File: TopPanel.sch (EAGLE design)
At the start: 19 parts

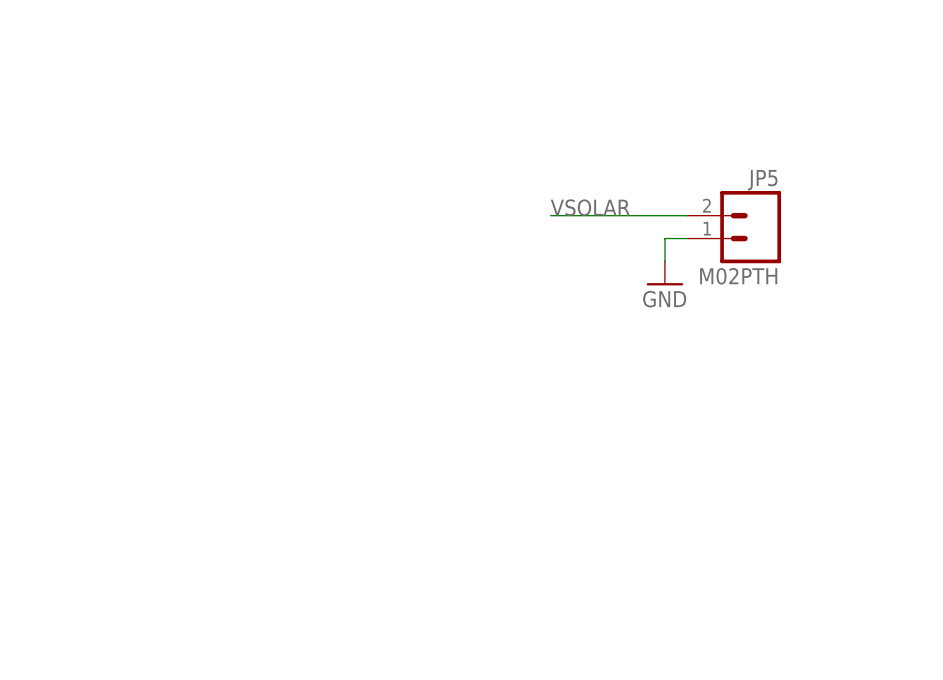
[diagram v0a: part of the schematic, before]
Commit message: Connector swap
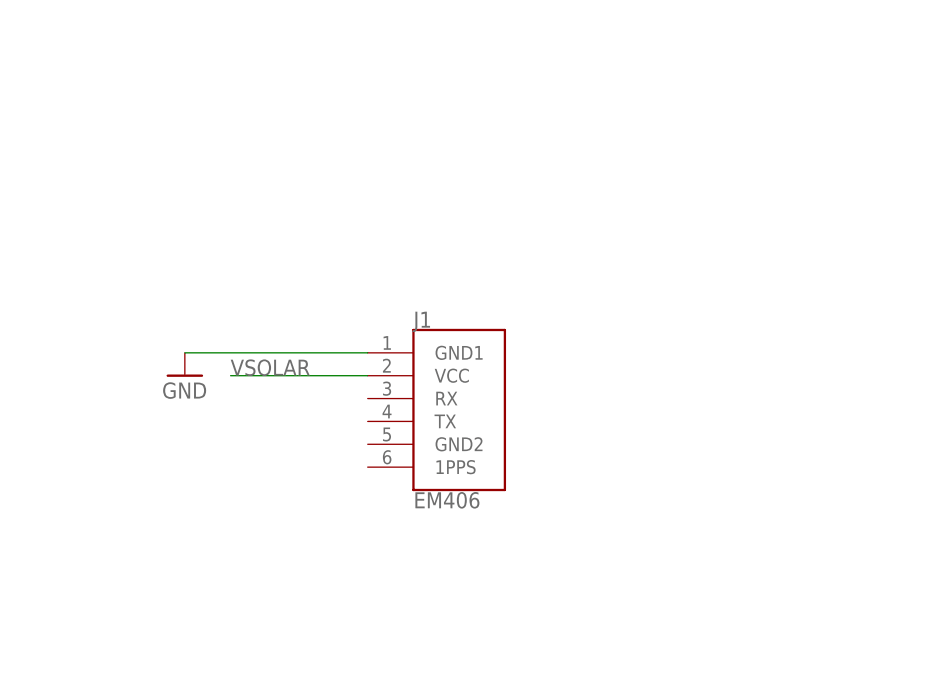
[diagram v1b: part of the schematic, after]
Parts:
- removed JP5: M02PTH, SparkFun-Connectors:M02PTH
- added J1: EM406, SparkFun-Connectors:EM406
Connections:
- net GND: now also J1.GND1; no longer JP5.1
- net VSOLAR: now also J1.VCC; no longer JP5.2
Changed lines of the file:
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@@
 <?xml version="1.0" encoding="utf-8"?>
 <!DOCTYPE eagle SYSTEM "eagle.dtd">
-<eagle version="8.6.1">
+<eagle version="9.1.3">
 <drawing>
 <settings>
@@
 <layers>
 <layer number="1" name="Top" color="4" fill="1" visible="no" active="no"/>
+<layer number="2" name="Route2" color="1" fill="3" visible="no" active="no"/>
+<layer number="3" name="Route3" color="4" fill="3" visible="no" active="no"/>
+<layer number="4" name="Route4" color="1" fill="4" visible="no" active="no"/>
+<layer number="5" name="Route5" color="4" fill="4" visible="no" active="no"/>
+<layer number="6" name="Route6" color="1" fill="8" visible="no" active="no"/>
+<layer number="7" name="Route7" color="4" fill="8" visible="no" active="no"/>
+<layer number="8" name="Route8" color="1" fill="2" visible="no" active="no"/>
+<layer number="9" name="Route9" color="4" fill="2" visible="no" active="no"/>
+<layer number="10" name="Route10" color="1" fill="7" visible="no" active="no"/>
+<layer number="11" name="Route11" color="4" fill="7" visible="no" active="no"/>
+<layer number="12" name="Route12" color="1" fill="5" visible="no" active="no"/>
+<layer number="13" name="Route13" color="4" fill="5" visible="no" active="no"/>
+<layer number="14" name="Route14" color="1" fill="6" visible="no" active="no"/>
+<layer number="15" name="Route15" color="4" fill="6" visible="no" active="no"/>
 <layer number="16" name="Bottom" color="1" fill="1" visible="no" active="no"/>
 <layer number="17" name="Pads" color="2" fill="1" visible="no" active="no"/>
@@
 <layer number="54" name="bGND_GNDA" color="1" fill="9" visible="no" active="no"/>
 <layer number="56" name="wert" color="7" fill="1" visible="no" active="no"/>
+<layer number="57" name="tCAD" color="7" fill="1" visible="no" active="no"/>
+<layer number="59" name="tCarbon" color="7" fill="1" visible="no" active="no"/>
+<layer number="60" name="bCarbon" color="7" fill="1" visible="no" active="no"/>
 <layer number="88" name="SimResults" color="9" fill="1" visible="yes" active="yes"/>
 <layer number="89" name="SimProbes" color="9" fill="1" visible="yes" active="yes"/>
@@
 <layer number="97" name="Info" color="7" fill="1" visible="yes" active="yes"/>
 <layer number="98" name="Guide" color="6" fill="1" visible="yes" active="yes"/>
+<layer number="99" name="SpiceOrder" color="7" fill="1" visible="yes" active="yes"/>
 <layer number="100" name="Muster" color="7" fill="1" visible="no" active="no"/>
 <layer number="101" name="Patch_Top" color="12" fill="4" visible="yes" active="yes"/>
@@
 <layer number="112" name="tSilk" color="7" fill="1" visible="yes" active="yes"/>
 <layer number="113" name="IDFDebug" color="4" fill="1" visible="yes" active="yes"/>
+<layer number="114" name="Badge_Outline" color="7" fill="1" visible="yes" active="yes"/>
+<layer number="115" name="ReferenceISLANDS" color="7" fill="1" visible="yes" active="yes"/>
 <layer number="116" name="Patch_BOT" color="9" fill="4" visible="yes" active="yes"/>
+<layer number="118" name="Rect_Pads" color="7" fill="1" visible="yes" active="yes"/>
 <layer number="121" name="_tsilk" color="7" fill="1" visible="yes" active="yes"/>
 <layer number="122" name="_bsilk" color="7" fill="1" visible="yes" active="yes"/>
@@
 <layer number="127" name="_tValues" color="7" fill="1" visible="yes" active="yes"/>
 <layer number="128" name="_bValues" color="7" fill="1" visible="yes" active="yes"/>
+<layer number="129" name="Mask" color="7" fill="1" visible="yes" active="yes"/>
 <layer number="131" name="tAdjust" color="7" fill="1" visible="yes" active="yes"/>
 <layer number="132" name="bAdjust" color="7" fill="1" visible="yes" active="yes"/>
 <layer number="144" name="Drill_legend" color="7" fill="1" visible="yes" active="yes"/>
+<layer number="150" name="Notes" color="7" fill="1" visible="yes" active="yes"/>
 <layer number="151" name="HeatSink" color="7" fill="1" visible="yes" active="yes"/>
 <layer number="152" name="_bDocu" color="7" fill="1" visible="yes" active="yes"/>
+<layer number="153" name="FabDoc1" color="7" fill="1" visible="yes" active="yes"/>
+<layer number="154" name="FabDoc2" color="7" fill="1" visible="yes" active="yes"/>
+<layer number="155" name="FabDoc3" color="7" fill="1" visible="yes" active="yes"/>
 <layer number="199" name="Contour" color="7" fill="1" visible="yes" active="yes"/>
 <layer number="200" name="200bmp" color="1" fill="10" visible="yes" active="yes"/>
@@
 <layer number="223" name="223bmp" color="24" fill="1" visible="no" active="no"/>
 <layer number="224" name="224bmp" color="25" fill="1" visible="no" active="no"/>
+<layer number="225" name="225bmp" color="7" fill="1" visible="yes" active="yes"/>
+<layer number="226" name="226bmp" color="7" fill="1" visible="yes" active="yes"/>
+<layer number="227" name="227bmp" color="7" fill="1" visible="yes" active="yes"/>
+<layer number="228" name="228bmp" color="7" fill="1" visible="yes" active="yes"/>
+<layer number="229" name="229bmp" color="7" fill="1" visible="yes" active="yes"/>
+<layer number="230" name="230bmp" color="7" fill="1" visible="yes" active="yes"/>
+<layer number="231" name="231bmp" color="7" fill="1" visible="yes" active="yes"/>
+<layer number="232" name="Eagle3D_PG2" color="7" fill="1" visible="yes" active="yes"/>
+<layer number="233" name="Eagle3D_PG3" color="7" fill="1" visible="yes" active="yes"/>
 <layer number="248" name="Housing" color="7" fill="1" visible="yes" active="yes"/>
 <layer number="249" name="Edge" color="7" fill="1" visible="yes" active="yes"/>
@@
 <layer number="251" name="SMDround" color="12" fill="11" visible="no" active="no"/>
 <layer number="254" name="cooling" color="7" fill="1" visible="yes" active="yes"/>
+<layer number="255" name="routoute" color="7" fill="1" visible="yes" active="yes"/>
 </layers>
 <schematic xreflabel="%F%N/%S.%C%R" xrefpart="/%S.%C%R">
@@
 <part name="GND1" library="SparkFun" deviceset="GND" device=""/>
 <part name="FRAME1" library="SparkFun-Aesthetics" deviceset="FRAME-LETTER" device=""/>
-<part name="JP5" library="SparkFun-Connectors" deviceset="M02" device="PTH"/>
-<part name="GND2" library="SparkFun" deviceset="GND" device=""/>
 <part name="U$1" library="KickSat-Logo" deviceset="KICKSAT_LOGO" device=""/>
+<part name="J1" library="SparkFun-Connectors" library_urn="urn:adsk.eagle:library:513" deviceset="EM406" device="" package3d_urn="urn:adsk.eagle:package:38023/1"/>
+<part name="GND3" library="SparkFun" deviceset="GND" device=""/>
 </parts>
 <sheets>
@@
 <instance part="FRAME1" gate="G$1" x="0" y="0"/>
 <instance part="FRAME1" gate="G$2" x="147.32" y="0"/>
-<instance part="JP5" gate="G$1" x="208.28" y="111.76" rot="MR0"/>
-<instance part="GND2" gate="1" x="198.12" y="106.68"/>
 <instance part="U$1" gate="G$1" x="218.44" y="25.4"/>
+<instance part="J1" gate="G$1" x="175.26" y="91.44"/>
+<instance part="GND3" gate="1" x="144.78" y="96.52"/>
 </instances>
 <busses>
@@
 </segment>
 <segment>
-<pinref part="JP5" gate="G$1" pin="2"/>
-<wire x1="200.66" y1="114.3" x2="185.42" y2="114.3" width="0.1524" layer="91"/>
-<label x="185.42" y="114.3" size="1.778" layer="95"/>
+<wire x1="165.1" y1="96.52" x2="149.86" y2="96.52" width="0.1524" layer="91"/>
+<pinref part="J1" gate="G$1" pin="VCC"/>
+<label x="149.86" y="96.52" size="1.778" layer="95"/>
 </segment>
 </net>
@@
 </segment>
 <segment>
-<pinref part="JP5" gate="G$1" pin="1"/>
-<pinref part="GND2" gate="1" pin="GND"/>
-<wire x1="200.66" y1="111.76" x2="198.12" y2="111.76" width="0.1524" layer="91"/>
-<wire x1="198.12" y1="111.76" x2="198.12" y2="109.22" width="0.1524" layer="91"/>
+<pinref part="J1" gate="G$1" pin="GND1"/>
+<pinref part="GND3" gate="1" pin="GND"/>
+<wire x1="165.1" y1="99.06" x2="144.78" y2="99.06" width="0.1524" layer="91"/>
 </segment>
 </net>
@@
 </schematic>
 </drawing>
+<compatibility>
+<note version="8.2" severity="warning">
+Since Version 8.2, EAGLE supports online libraries. The ids
+of those online libraries will not be understood (or retained)
+with this version.
+</note>
+<note version="8.3" severity="warning">
+Since Version 8.3, EAGLE supports URNs for individual library
+assets (packages, symbols, and devices). The URNs of those assets
+will not be understood (or retained) with this version.
+</note>
+<note version="8.3" severity="warning">
+Since Version 8.3, EAGLE supports the association of 3D packages
+with devices in libraries, schematics, and board files. Those 3D
+packages will not be understood (or retained) with this version.
+</note>
+</compatibility>
 </eagle>

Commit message: Started routing
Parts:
- added U$2, U$3, U$4: BURNWIRE, BurnWire:BURNWIRE
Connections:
- new net VBURN1: J1.VCC, U$2.V+
- new net VBURN2: J1.RX, U$3.V+
- new net VBURN3: J1.TX, U$4.V+
- net GND: now also J1.GND2, U$2.V-, U$3.V-, U$4.V-
- net VSOLAR: now also J1.1PPS; no longer J1.VCC
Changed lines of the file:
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@@
 <part name="J1" library="SparkFun-Connectors" library_urn="urn:adsk.eagle:library:513" deviceset="EM406" device="" package3d_urn="urn:adsk.eagle:package:38023/1"/>
 <part name="GND3" library="SparkFun" deviceset="GND" device=""/>
+<part name="GND2" library="SparkFun" deviceset="GND" device=""/>
+<part name="GND4" library="SparkFun" deviceset="GND" device=""/>
+<part name="GND5" library="SparkFun" deviceset="GND" device=""/>
+<part name="GND6" library="SparkFun" deviceset="GND" device=""/>
+<part name="U$2" library="BurnWire" deviceset="BURNWIRE" device=""/>
+<part name="U$3" library="BurnWire" deviceset="BURNWIRE" device=""/>
+<part name="U$4" library="BurnWire" deviceset="BURNWIRE" device=""/>
 </parts>
 <sheets>
@@
 <instance part="J1" gate="G$1" x="175.26" y="91.44"/>
 <instance part="GND3" gate="1" x="144.78" y="96.52"/>
+<instance part="GND2" gate="1" x="144.78" y="86.36"/>
+<instance part="GND4" gate="1" x="111.76" y="58.42"/>
+<instance part="GND5" gate="1" x="111.76" y="48.26"/>
+<instance part="GND6" gate="1" x="111.76" y="38.1"/>
+<instance part="U$2" gate="G$1" x="127" y="60.96"/>
+<instance part="U$3" gate="G$1" x="127" y="50.8"/>
+<instance part="U$4" gate="G$1" x="127" y="40.64"/>
 </instances>
 <busses>
@@
 </segment>
 <segment>
-<wire x1="165.1" y1="96.52" x2="149.86" y2="96.52" width="0.1524" layer="91"/>
-<pinref part="J1" gate="G$1" pin="VCC"/>
-<label x="149.86" y="96.52" size="1.778" layer="95"/>
+<pinref part="J1" gate="G$1" pin="1PPS"/>
+<wire x1="165.1" y1="86.36" x2="149.86" y2="86.36" width="0.1524" layer="91"/>
+<label x="149.86" y="86.36" size="1.778" layer="95"/>
 </segment>
 </net>
@@
 <wire x1="165.1" y1="99.06" x2="144.78" y2="99.06" width="0.1524" layer="91"/>
 </segment>
-</net>
+<segment>
+<pinref part="J1" gate="G$1" pin="GND2"/>
+<wire x1="165.1" y1="88.9" x2="147.32" y2="88.9" width="0.1524" layer="91"/>
+<pinref part="GND2" gate="1" pin="GND"/>
+<wire x1="147.32" y1="88.9" x2="144.78" y2="88.9" width="0.1524" layer="91"/>
+</segment>
+<segment>
+<pinref part="GND4" gate="1" pin="GND"/>
+<wire x1="114.3" y1="60.96" x2="111.76" y2="60.96" width="0.1524" layer="91"/>
+<pinref part="U$2" gate="G$1" pin="V-"/>
+</segment>
+<segment>
+<pinref part="GND5" gate="1" pin="GND"/>
+<wire x1="114.3" y1="50.8" x2="111.76" y2="50.8" width="0.1524" layer="91"/>
+<pinref part="U$3" gate="G$1" pin="V-"/>
+</segment>
+<segment>
+<pinref part="GND6" gate="1" pin="GND"/>
+<wire x1="114.3" y1="40.64" x2="111.76" y2="40.64" width="0.1524" layer="91"/>
+<pinref part="U$4" gate="G$1" pin="V-"/>
+</segment>
+</net>
+<net name="VBURN1" class="0">
+<segment>
+<pinref part="J1" gate="G$1" pin="VCC"/>
+<wire x1="165.1" y1="96.52" x2="149.86" y2="96.52" width="0.1524" layer="91"/>
+<label x="149.86" y="96.52" size="1.778" layer="95"/>
+</segment>
+<segment>
+<wire x1="139.7" y1="60.96" x2="149.86" y2="60.96" width="0.1524" layer="91"/>
+<label x="139.7" y="60.96" size="1.778" layer="95"/>
+<pinref part="U$2" gate="G$1" pin="V+"/>
+</segment>
+</net>
+<net name="VBURN2" class="0">
+<segment>
+<pinref part="J1" gate="G$1" pin="RX"/>
+<wire x1="165.1" y1="93.98" x2="149.86" y2="93.98" width="0.1524" layer="91"/>
+<label x="149.86" y="93.98" size="1.778" layer="95"/>
+</segment>
+<segment>
+<wire x1="139.7" y1="50.8" x2="149.86" y2="50.8" width="0.1524" layer="91"/>
+<label x="139.7" y="50.8" size="1.778" layer="95"/>
+<pinref part="U$3" gate="G$1" pin="V+"/>
+</segment>
+</net>
+<net name="VBURN3" class="0">
+<segment>
+<pinref part="J1" gate="G$1" pin="TX"/>
+<wire x1="165.1" y1="91.44" x2="149.86" y2="91.44" width="0.1524" layer="91"/>
+<label x="149.86" y="91.44" size="1.778" layer="95"/>
+</segment>
+<segment>
+<wire x1="139.7" y1="40.64" x2="149.86" y2="40.64" width="0.1524" layer="91"/>
+<label x="139.7" y="40.64" size="1.778" layer="95"/>
+<pinref part="U$4" gate="G$1" pin="V+"/>
+</segment>
+</net>

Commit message: Finished layout
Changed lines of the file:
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@@
 <instance part="GND3" gate="1" x="144.78" y="96.52"/>
 <instance part="GND2" gate="1" x="144.78" y="86.36"/>
-<instance part="GND4" gate="1" x="111.76" y="58.42"/>
-<instance part="GND5" gate="1" x="111.76" y="48.26"/>
-<instance part="GND6" gate="1" x="111.76" y="38.1"/>
-<instance part="U$2" gate="G$1" x="127" y="60.96"/>
-<instance part="U$3" gate="G$1" x="127" y="50.8"/>
-<instance part="U$4" gate="G$1" x="127" y="40.64"/>
+<instance part="GND4" gate="1" x="144.78" y="149.86"/>
+<instance part="GND5" gate="1" x="144.78" y="139.7"/>
+<instance part="GND6" gate="1" x="144.78" y="129.54"/>
+<instance part="U$2" gate="G$1" x="160.02" y="152.4"/>
+<instance part="U$3" gate="G$1" x="160.02" y="142.24"/>
+<instance part="U$4" gate="G$1" x="160.02" y="132.08"/>
 </instances>
 <busses>
@@
 <segment>
 <pinref part="GND4" gate="1" pin="GND"/>
-<wire x1="114.3" y1="60.96" x2="111.76" y2="60.96" width="0.1524" layer="91"/>
+<wire x1="147.32" y1="152.4" x2="144.78" y2="152.4" width="0.1524" layer="91"/>
 <pinref part="U$2" gate="G$1" pin="V-"/>
 </segment>
 <segment>
 <pinref part="GND5" gate="1" pin="GND"/>
-<wire x1="114.3" y1="50.8" x2="111.76" y2="50.8" width="0.1524" layer="91"/>
+<wire x1="147.32" y1="142.24" x2="144.78" y2="142.24" width="0.1524" layer="91"/>
 <pinref part="U$3" gate="G$1" pin="V-"/>
 </segment>
 <segment>
 <pinref part="GND6" gate="1" pin="GND"/>
-<wire x1="114.3" y1="40.64" x2="111.76" y2="40.64" width="0.1524" layer="91"/>
+<wire x1="147.32" y1="132.08" x2="144.78" y2="132.08" width="0.1524" layer="91"/>
 <pinref part="U$4" gate="G$1" pin="V-"/>
 </segment>
@@
 </segment>
 <segment>
-<wire x1="139.7" y1="60.96" x2="149.86" y2="60.96" width="0.1524" layer="91"/>
-<label x="139.7" y="60.96" size="1.778" layer="95"/>
+<wire x1="172.72" y1="152.4" x2="182.88" y2="152.4" width="0.1524" layer="91"/>
+<label x="172.72" y="152.4" size="1.778" layer="95"/>
 <pinref part="U$2" gate="G$1" pin="V+"/>
 </segment>
@@
 </segment>
 <segment>
-<wire x1="139.7" y1="50.8" x2="149.86" y2="50.8" width="0.1524" layer="91"/>
-<label x="139.7" y="50.8" size="1.778" layer="95"/>
+<wire x1="172.72" y1="142.24" x2="182.88" y2="142.24" width="0.1524" layer="91"/>
+<label x="172.72" y="142.24" size="1.778" layer="95"/>
 <pinref part="U$3" gate="G$1" pin="V+"/>
 </segment>
@@
 </segment>
 <segment>
-<wire x1="139.7" y1="40.64" x2="149.86" y2="40.64" width="0.1524" layer="91"/>
-<label x="139.7" y="40.64" size="1.778" layer="95"/>
+<wire x1="172.72" y1="132.08" x2="182.88" y2="132.08" width="0.1524" layer="91"/>
+<label x="172.72" y="132.08" size="1.778" layer="95"/>
 <pinref part="U$4" gate="G$1" pin="V+"/>
 </segment>
